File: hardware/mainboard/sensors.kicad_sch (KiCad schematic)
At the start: 3 parts

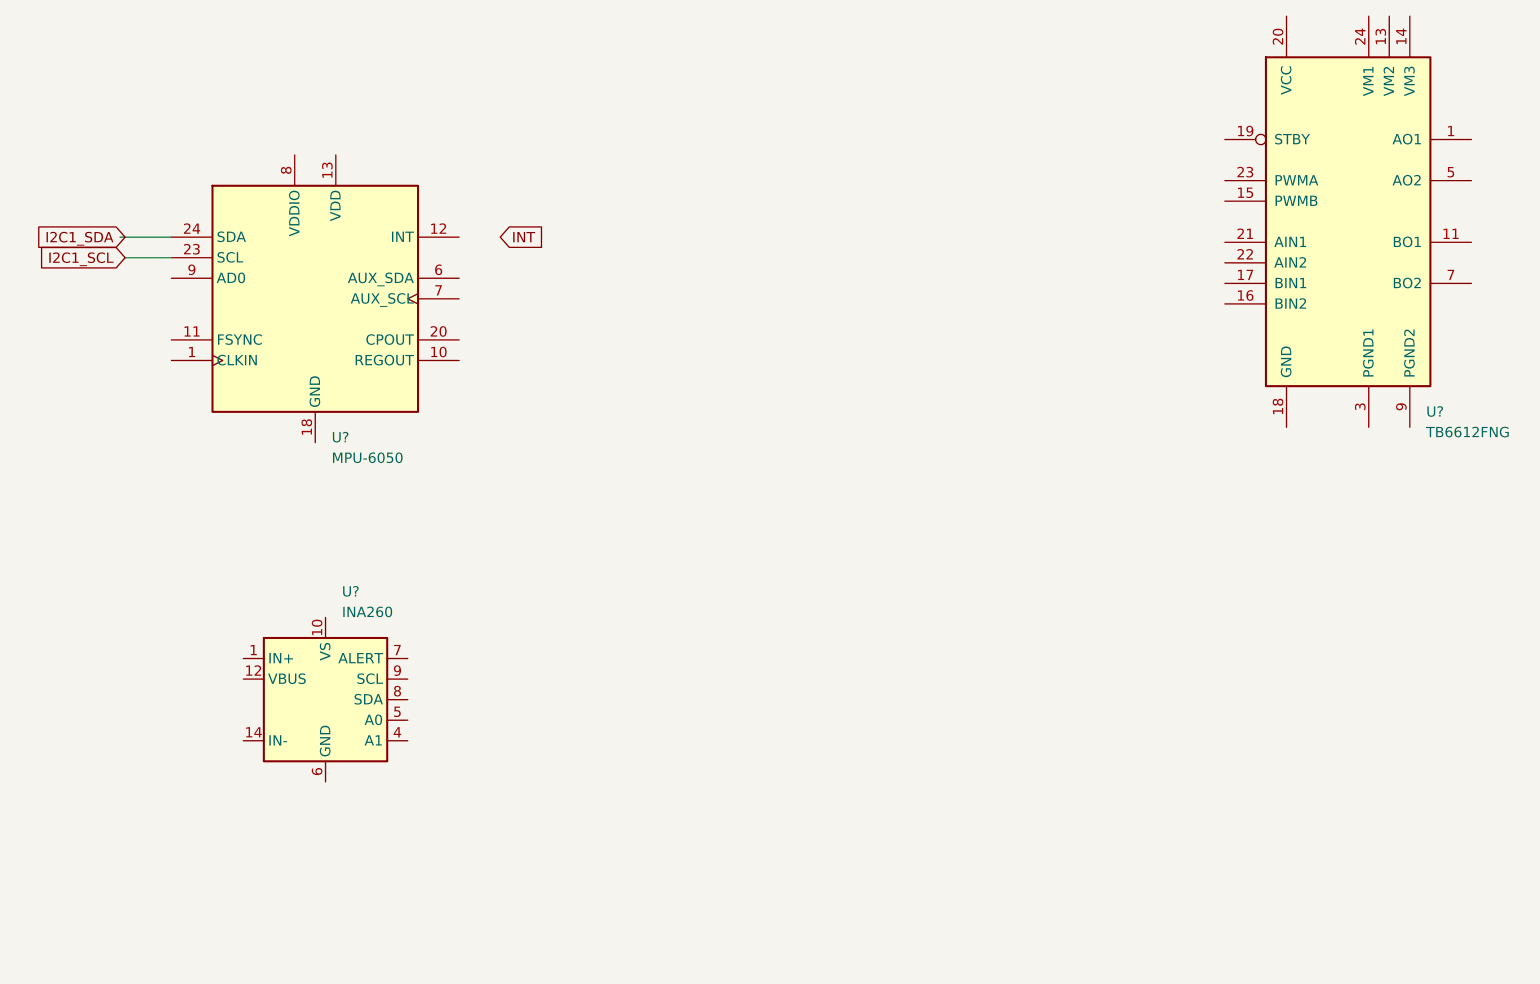
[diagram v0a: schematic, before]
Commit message: Added Jy-901 Bluetooth and Wifi
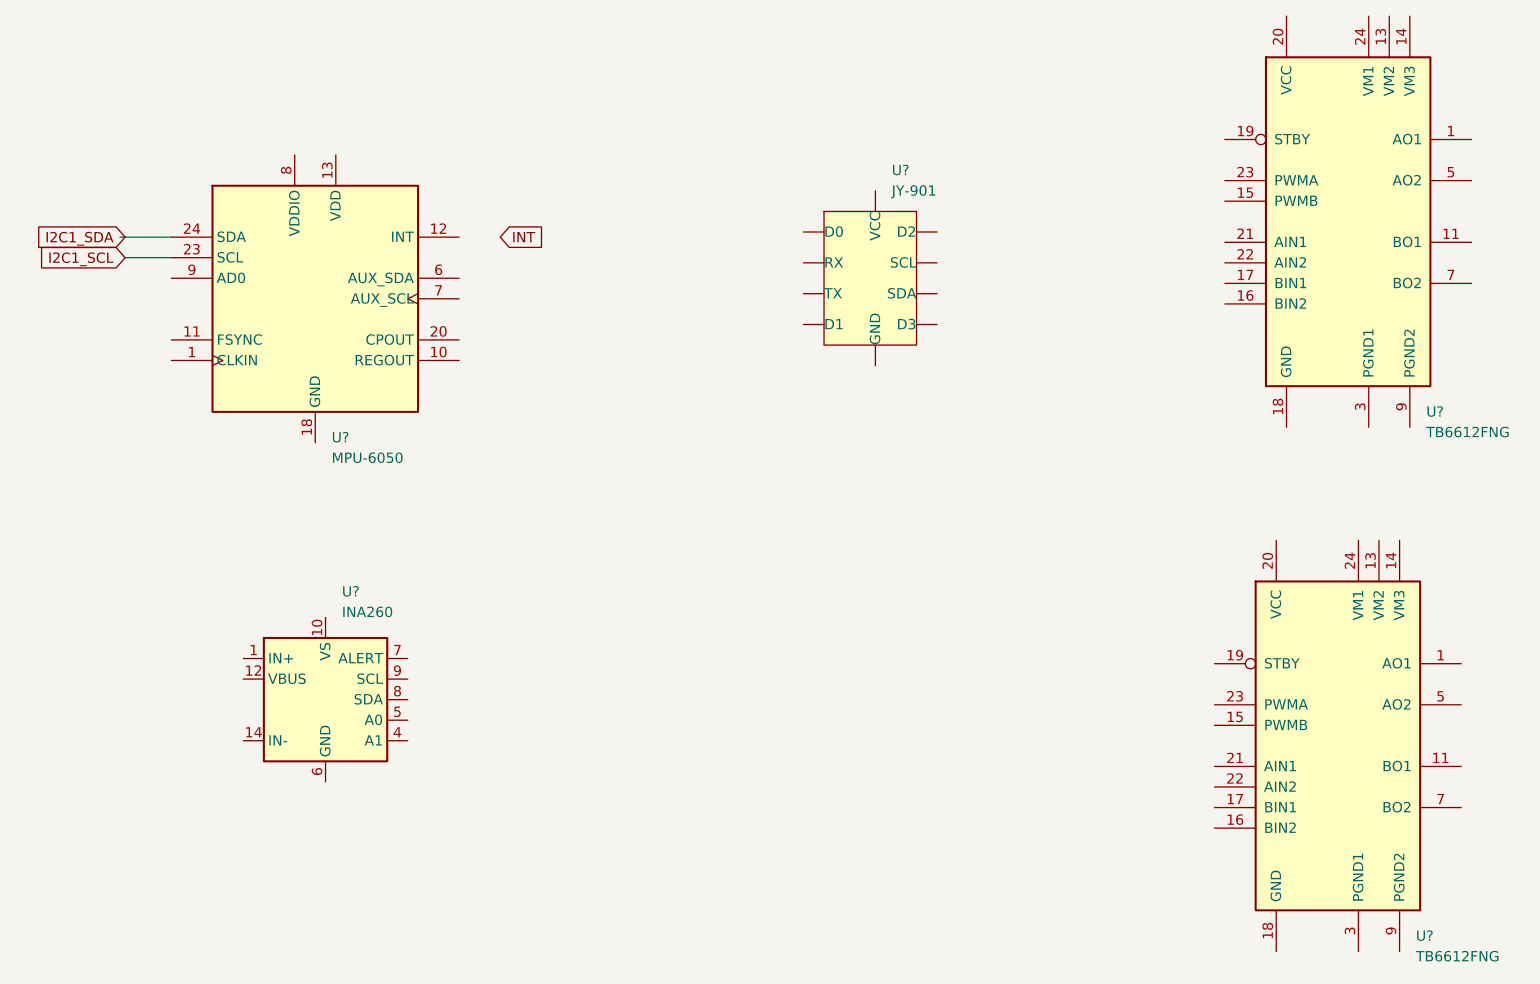
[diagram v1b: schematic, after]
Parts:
- added U?: TB6612FNG, Package_SO:SSOP-24_5.3x8.2mm_P0.65mm, symbol Driver_Motor:TB6612FNG
- added U?: JY-901, symbol sensors:JY-901
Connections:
- new net: U?.1 (AO1), U?.2 (AO1)
- new net: U?.10 (PGND2), U?.9 (PGND2)
- new net: U?.11 (BO1), U?.12 (BO1)
- new net: U?.3 (PGND1), U?.4 (PGND1)
- new net: U?.5 (AO2), U?.6 (AO2)
- new net: U?.7 (BO2), U?.8 (BO2)
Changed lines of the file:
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@@
     )
+  )
+  (symbol (lib_id "Driver_Motor:TB6612FNG") (at 194.31 125.73 0) (unit 1)
+    (in_bom yes) (on_board yes) (fields_autoplaced)
+    (property "Reference" "U?" (id 0) (at 203.9494 149.225 0)
+      (effects (font (size 1.27 1.27)) (justify left))
+    )
+    (property "Value" "TB6612FNG" (id 1) (at 203.9494 151.765 0)
+      (effects (font (size 1.27 1.27)) (justify left))
+    )
+    (property "Footprint" "Package_SO:SSOP-24_5.3x8.2mm_P0.65mm" (id 2) (at 227.33 148.59 0)
+      (effects (font (size 1.27 1.27)) hide)
+    )
+    (property "Datasheet" "https://toshiba.semicon-storage.com/us/product/linear/motordriver/detail.TB6612FNG.html" (id 3) (at 205.74 110.49 0)
+      (effects (font (size 1.27 1.27)) hide)
+    )
+    (pin "1")
+    (pin "10")
+    (pin "11")
+    (pin "12")
+    (pin "13")
+    (pin "14")
+    (pin "15")
+    (pin "16")
+    (pin "17")
+    (pin "18")
+    (pin "19")
+    (pin "2")
+    (pin "20")
+    (pin "21")
+    (pin "22")
+    (pin "23")
+    (pin "24")
+    (pin "3")
+    (pin "4")
+    (pin "5")
+    (pin "6")
+    (pin "7")
+    (pin "8")
+    (pin "9")
   )
   (symbol (lib_id "Sensor:INA260") (at 69.215 120.015 0) (unit 1)
@@
     (pin "9")
   )
+  (symbol (lib_id "sensors:JY-901") (at 120.65 77.47 0) (unit 1)
+    (in_bom yes) (on_board yes) (fields_autoplaced)
+    (property "Reference" "U?" (id 0) (at 139.1794 54.61 0)
+      (effects (font (size 1.27 1.27)) (justify left))
+    )
+    (property "Value" "JY-901" (id 1) (at 139.1794 57.15 0)
+      (effects (font (size 1.27 1.27)) (justify left))
+    )
+    (property "Footprint" "" (id 2) (at 120.65 77.47 0)
+      (effects (font (size 1.27 1.27)) hide)
+    )
+    (property "Datasheet" "" (id 3) (at 120.65 77.47 0)
+      (effects (font (size 1.27 1.27)) hide)
+    )
+    (pin "")
+    (pin "")
+    (pin "")
+    (pin "")
+    (pin "")
+    (pin "")
+    (pin "")
+    (pin "")
+    (pin "")
+    (pin "")
+  )
 )
